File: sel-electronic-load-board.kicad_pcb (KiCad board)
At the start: 4 copper layers, 0 parts

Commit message: start laying out components : connectors and DMM bypass toggle
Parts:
- added C1: 0.1uF, Capacitor_SMD:C_1206_3216Metric_Pad1.33x1.80mm_HandSolder, F.Cu at (280.0, 70.0)
- added C2: 0.1uF, Capacitor_SMD:C_1206_3216Metric_Pad1.33x1.80mm_HandSolder, F.Cu at (266.0, 80.2)
- added C3: 0.1uF, Capacitor_SMD:C_1206_3216Metric_Pad1.33x1.80mm_HandSolder, F.Cu at (272.9, 75.5)
- added C4: 0.1uF, Capacitor_SMD:C_1206_3216Metric_Pad1.33x1.80mm_HandSolder, F.Cu at (261.9, 87.9)
- added C5: 0.1uF, Capacitor_SMD:C_1206_3216Metric_Pad1.33x1.80mm_HandSolder, F.Cu at (255.8, 87.9)
- added F1: Fuse 4A, Fuse:Fuseholder_Cylinder-5x20mm_Stelvio-Kontek_PTF78_Horizontal_Open, F.Cu at (210.8, 47.1)
- added H1: DUT+, MountingHole:MountingHole_4.3mm_M4_Pad, F.Cu at (150.0, 57.0)
- added H2: DUT-, MountingHole:MountingHole_4.3mm_M4_Pad, F.Cu at (165.0, 57.0)
- added H3: DMM+, MountingHole:MountingHole_4.3mm_M4_Pad, F.Cu at (193.0, 110.0)
- added H4: DMM-, MountingHole:MountingHole_4.3mm_M4_Pad, F.Cu at (193.0, 125.0)
- added H5: MountingHole, MountingHole:MountingHole_4.3mm_M4, F.Cu at (55.0, 55.0)
- added H6: MountingHole, MountingHole:MountingHole_4.3mm_M4, F.Cu at (195.0, 55.0)
- added H7: MountingHole, MountingHole:MountingHole_4.3mm_M4, F.Cu at (55.0, 145.0)
- added H8: MountingHole, MountingHole:MountingHole_4.3mm_M4, F.Cu at (195.0, 145.0)
- added J1: HE10 receptacle, Connector_IDC:IDC-Header_2x05_P2.54mm_Horizontal, F.Cu at (186.0, 67.0)
- added JP1: If needed by the IC, Jumper:SolderJumper-2_P1.3mm_Open_RoundedPad1.0x1.5mm, F.Cu at (227.8, 72.2)
- added Q1: N-mosfet, Package_TO_SOT_THT:TO-220-3_Vertical, F.Cu at (211.7, 84.9)
- added Q10: N-mosfet, Package_TO_SOT_THT:TO-220-3_Vertical, F.Cu at (240.4, 61.3)
- added Q11: N-mosfet, Package_TO_SOT_THT:TO-220-3_Vertical, F.Cu at (252.0, 57.5)
- added Q12: N-mosfet, Package_TO_SOT_THT:TO-220-3_Vertical, F.Cu at (234.8, 74.4)
- added Q13: N-mosfet, Package_TO_SOT_THT:TO-220-3_Vertical, F.Cu at (223.2, 84.9)
- added Q14: N-mosfet, Package_TO_SOT_THT:TO-220-3_Vertical, F.Cu at (254.6, 51.5)
- added Q15: N-mosfet, Package_TO_SOT_THT:TO-220-3_Vertical, F.Cu at (266.2, 45.5)
- added Q16: N-mosfet, Package_TO_SOT_THT:TO-220-3_Vertical, F.Cu at (266.2, 51.5)
- added Q2: N-mosfet, Package_TO_SOT_THT:TO-220-3_Vertical, F.Cu at (240.4, 55.3)
- added Q3: N-mosfet, Package_TO_SOT_THT:TO-220-3_Vertical, F.Cu at (228.9, 68.4)
- added Q4: N-mosfet, Package_TO_SOT_THT:TO-220-3_Vertical, F.Cu at (254.6, 45.5)
- added Q5: N-mosfet, Package_TO_SOT_THT:TO-220-3_Vertical, F.Cu at (228.9, 62.5)
- added Q6: N-mosfet, Package_TO_SOT_THT:TO-220-3_Vertical, F.Cu at (228.9, 56.5)
- added Q7: N-mosfet, Package_TO_SOT_THT:TO-220-3_Vertical, F.Cu at (223.2, 78.9)
- added Q8: N-mosfet, Package_TO_SOT_THT:TO-220-3_Vertical, F.Cu at (211.7, 78.9)
- added Q9: N-mosfet, Package_TO_SOT_THT:TO-220-3_Vertical, F.Cu at (240.4, 67.2)
- added RN1: 10K, Resistor_SMD:R_Array_Convex_4x0603, F.Cu at (271.1, 80.9)
- added RN2: 10K, Resistor_SMD:R_Array_Convex_4x0603, F.Cu at (245.2, 71.6)
- added RN3: 10K, Resistor_SMD:R_Array_Convex_4x0603, F.Cu at (279.1, 74.0)
- added RV1: 50K, Potentiometer_THT:Potentiometer_Bourns_3296Y_Vertical, F.Cu at (239.7, 84.7)
- added RV2: 50K, Potentiometer_THT:Potentiometer_Bourns_3296Y_Vertical, F.Cu at (282.6, 43.5)
- added RV3: 50K, Potentiometer_THT:Potentiometer_Bourns_3296Y_Vertical, F.Cu at (239.7, 78.3)
- added RV4: 50K, Potentiometer_THT:Potentiometer_Bourns_3296Y_Vertical, F.Cu at (256.9, 61.4)
- added SW1: DMM bypass, switches:toggle-switch-P4.70mm-3pins-75mils-vias, F.Cu at (193.0, 93.0)
- added U1: OpAmp, Package_SO:TSSOP-8_3x3mm_P0.65mm, F.Cu at (266.5, 76.2)
- added U2: Input stage, Package_SO:TSSOP-8_3x3mm_P0.65mm, F.Cu at (273.5, 70.7)
- added U3: Output stage, Package_SO:TSSOP-8_3x3mm_P0.65mm, F.Cu at (289.1, 44.0)
- added U4: Current sensor, Package_SO:SOIC-8_3.9x4.9mm_P1.27mm, F.Cu at (288.9, 51.2)
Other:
- board outline added: 150 x 100 mm
- board text added: "Bypass DMM"

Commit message: reorganize copper pour, traces, DMM and bypass, connector to main board
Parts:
- moved Q4 187.7 mm to (68.0, 66.0), turned to 90 degrees
- moved Q2 182.8 mm to (68.0, 116.0), turned to 90 degrees
- moved Q5 165.7 mm to (83.0, 141.0), turned to 90 degrees
- moved Q3 162.5 mm to (68.0, 91.0), turned to 90 degrees
- moved RV2 160.6 mm to (155.0, 141.0)
- moved Q9 160.4 mm to (98.0, 141.0), turned to 90 degrees
- moved Q15 159.8 mm to (113.0, 91.0), turned to 90 degrees
- moved Q11 157.6 mm to (98.0, 91.0), turned to 90 degrees
- moved Q6 157.5 mm to (83.0, 116.0), turned to 90 degrees
- moved Q14 155.6 mm to (113.0, 116.0), turned to 90 degrees
- moved Q1 154.2 mm to (68.0, 141.0), turned to 90 degrees
- moved Q16 153.8 mm to (113.0, 66.0), turned to 90 degrees
- moved Q10 152.6 mm to (98.0, 116.0), turned to 90 degrees
- moved U3 145.1 mm to (162.0, 114.0)
- moved C1 144.7 mm to (147.0, 127.0), turned to 180 degrees
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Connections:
- RN1 pad 1: Net-(RN1-Pad1) -> /SINK_CMD
- RN1 pad 5: /SINK_CMD -> Net-(RN1-Pad5)
- RN1 pad 6: Net-(RN1-Pad4) -> Net-(RN1-Pad5)
- RN2 pad 1: Net-(RN1-Pad3) -> Net-(RN1-Pad2)
- RN2 pad 8: Net-(RN1-Pad7) -> Net-(RN1-Pad5)
- RV1 pad 2: Net-(RN1-Pad1) -> Net-(RN1-Pad3)
- RV2 pad 2: Net-(RN1-Pad2) -> Net-(RN1-Pad4)
- U1 pad 1: Net-(RN1-Pad3) -> Net-(RN1-Pad2)
- U1 pad 2: Net-(RN1-Pad7) -> Net-(RN1-Pad5)
- U1 pad 6: Net-(RN1-Pad4) -> Net-(RN1-Pad7)
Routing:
- net /SINK+: track 0.00 -> 425.1 mm
- net /SINK_CMD: track 0.00 -> 284.6 mm
- net Net-(F1-Pad1): track 0.00 -> 102.7 mm
- net Net-(H4-Pad1): track 0.00 -> 78.4 mm
- net Net-(RN1-Pad4): track 0.00 -> 19.5 mm
- net Net-(RN1-Pad2): track 0.00 -> 16.5 mm
- net Net-(RN1-Pad3): track 0.00 -> 15.3 mm
- net GND: track 0.00 -> 13.7 mm, vias 0 -> 6
- net Net-(F1-Pad2): track 0.00 -> 11.4 mm
- net Net-(RN1-Pad5): track 0.00 -> 11.4 mm
- net VCC: track 0.00 -> 6.08 mm, vias 0 -> 2
- net Net-(RN1-Pad7): track 0.00 -> 5.91 mm
- net Net-(JP1-Pad2): track 0.00 -> 3.11 mm
- added copper zone on F.Cu, net /SINK+
- added copper zone on In1.Cu, net GND
- added copper zone on F.Cu, net VCC
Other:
- net class 2A: clearance 0.2 -> 0.3
- net class 3A: clearance 0.2 -> 0.4
- net class 4A: clearance 0.2 -> 0.5
- board text added: "Bias"
- board text added: "Command"
- board text added: "Gain"
- board text added: "Monitoring"
- board text added: "Offset"
- board text added: "Scale"

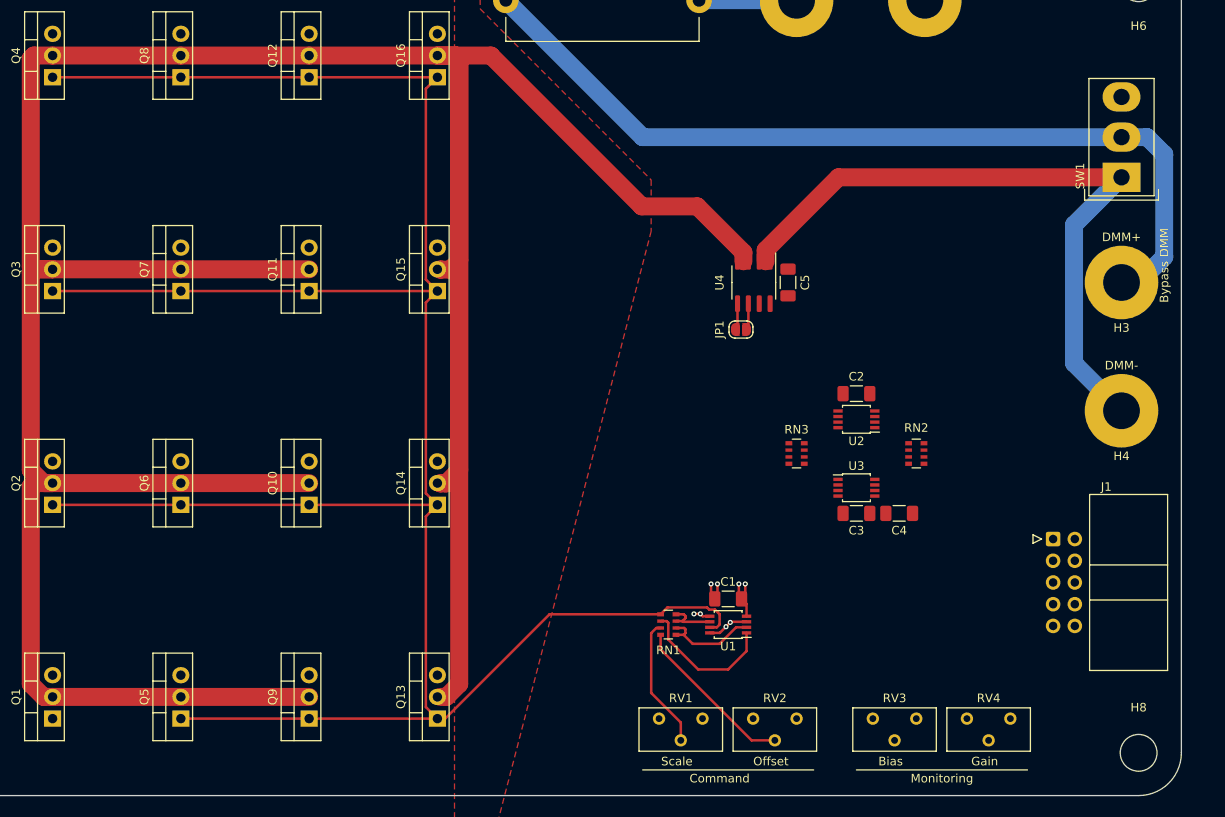
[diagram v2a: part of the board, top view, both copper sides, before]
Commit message: done tracing, optimizing the use of network resistors units
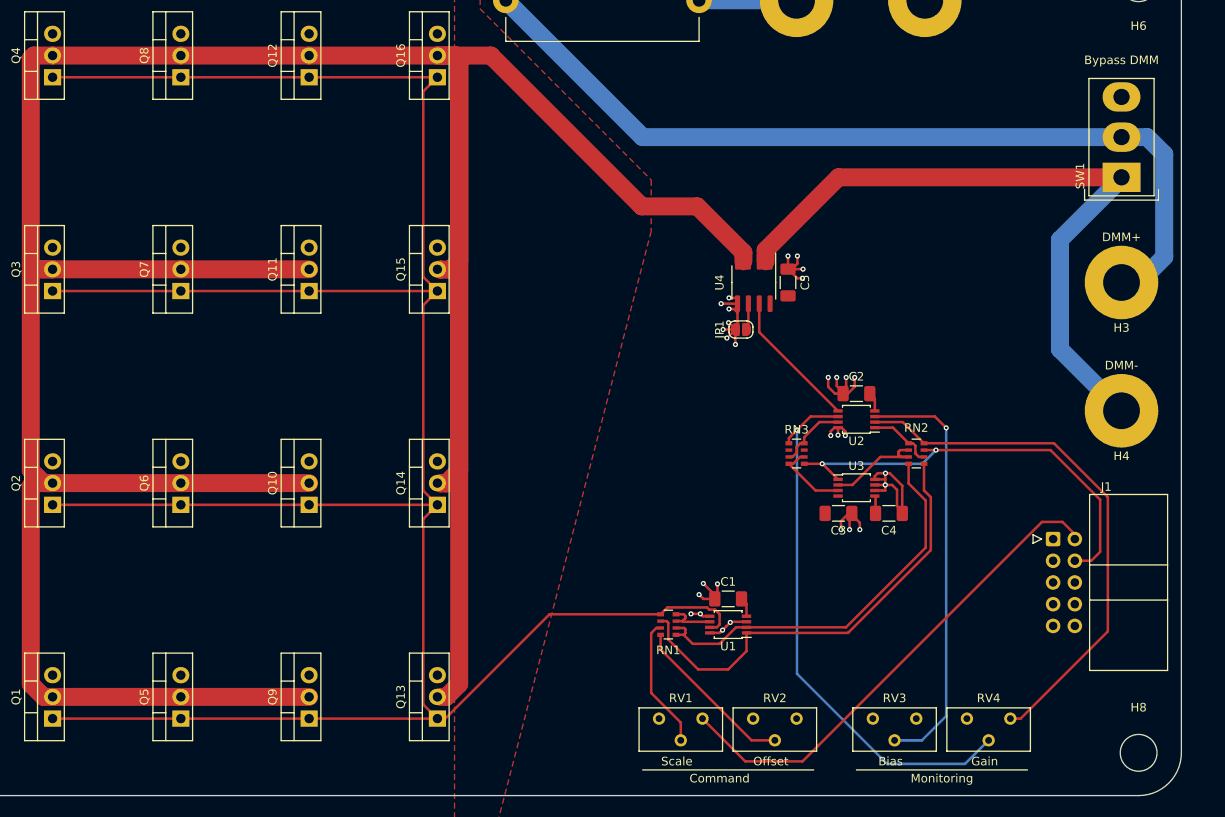
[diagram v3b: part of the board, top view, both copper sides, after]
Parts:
- moved C3 2.10 mm to (159.9, 117.0)
- moved C4 1.20 mm to (165.8, 117.0)
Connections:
- RN2 pad 4: Net-(RN2-Pad2) -> Net-(RN2-Pad4)
- RN2 pad 5: Net-(RN2-Pad5) -> Net-(RN2-Pad2)
- RN3 pad 2: Net-(RN3-Pad1) -> Net-(RN3-Pad2)
- RN3 pad 3: /UC_ADC -> Net-(RN3-Pad3)
- RN3 pad 4: (no net) -> Net-(RN3-Pad4)
- RN3 pad 5: (no net) -> /UC_ADC
- RN3 pad 6: Net-(RN3-Pad6) -> Net-(RN3-Pad4)
- RN3 pad 7: Net-(RN3-Pad6) -> Net-(RN3-Pad7)
- RN3 pad 8: Net-(RN3-Pad8) -> Net-(RN3-Pad3)
- RV4 pad 1: Net-(RN2-Pad5) -> Net-(RN2-Pad4)
- RV4 pad 2: Net-(RN3-Pad8) -> Net-(RN3-Pad1)
- U2 pad 2: Net-(RN2-Pad5) -> Net-(RN2-Pad4)
- U2 pad 6: Net-(RN3-Pad8) -> Net-(RN3-Pad1)
- U2 pad 7: Net-(RN3-Pad1) -> Net-(RN3-Pad3)
- U3 pad 3: Net-(RN3-Pad6) -> Net-(RN3-Pad4)
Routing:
- net Net-(RN3-Pad1): track 0.00 -> 63.8 mm, vias 0 -> 1
- net Net-(RN2-Pad4): track 0.00 -> 62.2 mm
- net GND: track 13.7 -> 73.7 mm, vias 6 -> 30
- net /UC_DAC: track 0.00 -> 58.4 mm
- net /UC_ADC: track 0.00 -> 51.2 mm, vias 0 -> 2
- net Net-(RV3-Pad2): track 0.00 -> 49.8 mm, vias 0 -> 1
- net Net-(RN1-Pad2): track 16.5 -> 52.5 mm
- net Net-(RN1-Pad5): track 11.4 -> 46.8 mm
- net /V_SENSE: track 0.00 -> 16.4 mm
- net /SINK_CMD: track 284.6 -> 300.3 mm
- net Net-(RN2-Pad6): track 0.00 -> 12.5 mm
- net Net-(RN3-Pad4): track 0.00 -> 9.18 mm
- net Net-(RN3-Pad3): track 0.00 -> 8.23 mm
- net Net-(RN2-Pad2): track 0.00 -> 7.70 mm
- net Net-(C4-Pad1): track 0.00 -> 2.06 mm
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
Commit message: prepare first release
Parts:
- added G***: LOGO, cliparts:logo--cc--zero, F.Cu at (125.0, 100.0)
- added G***: LOGO, cliparts:logo--cc--cc, F.Cu at (120.0, 100.0)
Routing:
- net VCC: vias 0 -> 3
- net GND: vias 30 -> 33
- added copper zone on B.Cu, net /SINK+
- added copper zone on In2.Cu, net GND
- added copper zone on B.Cu, net VCC
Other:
- board text added: "WITHOUT ANY WARRANTY OF ANY KIND, INCLUDING, BUT NOT LIMITED TO, THE IMPLIED WARRANTIES OF SAFETY, MERCHANTABILITY AND FITNESS FOR A PARTICULAR PURPOSE."
- board text added: "https://github.com/sporniket/sel-electronic-load-board v0.0.1"

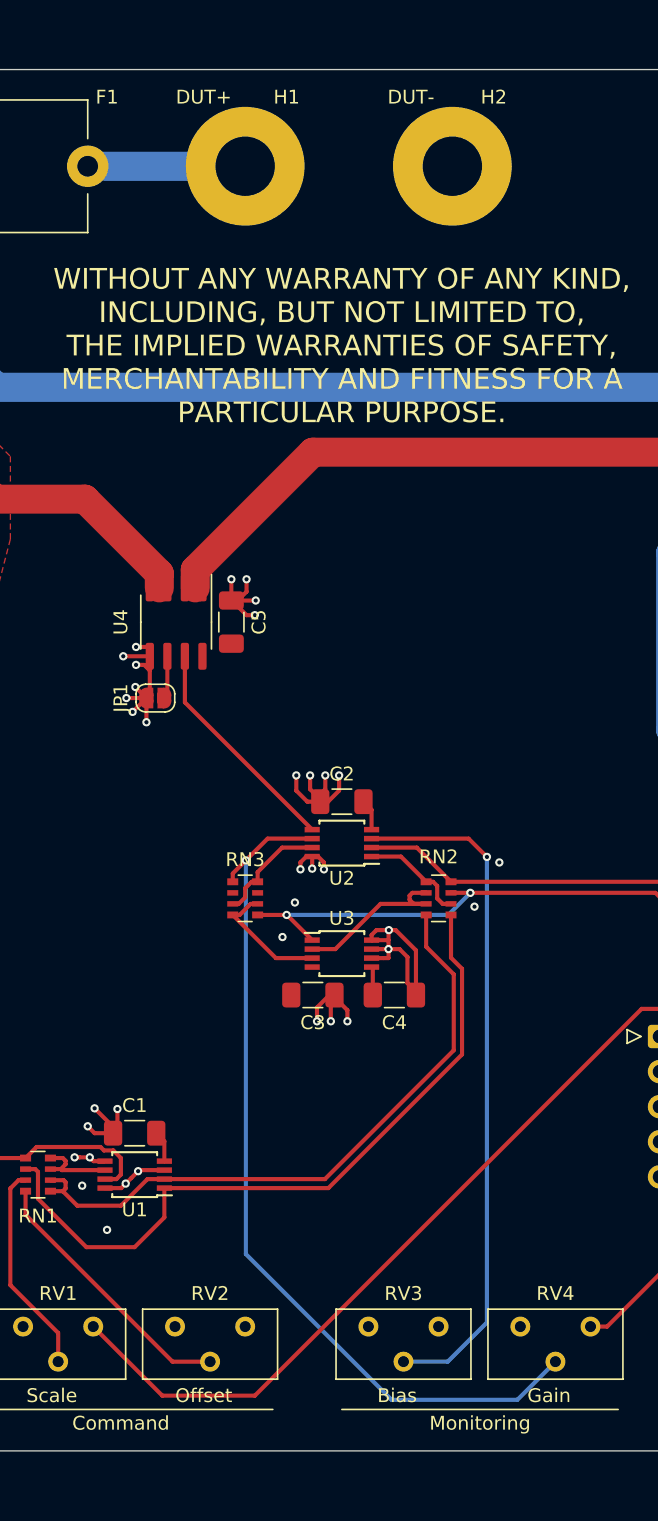
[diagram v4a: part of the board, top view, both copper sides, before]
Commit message: adjust labels on silkscreen
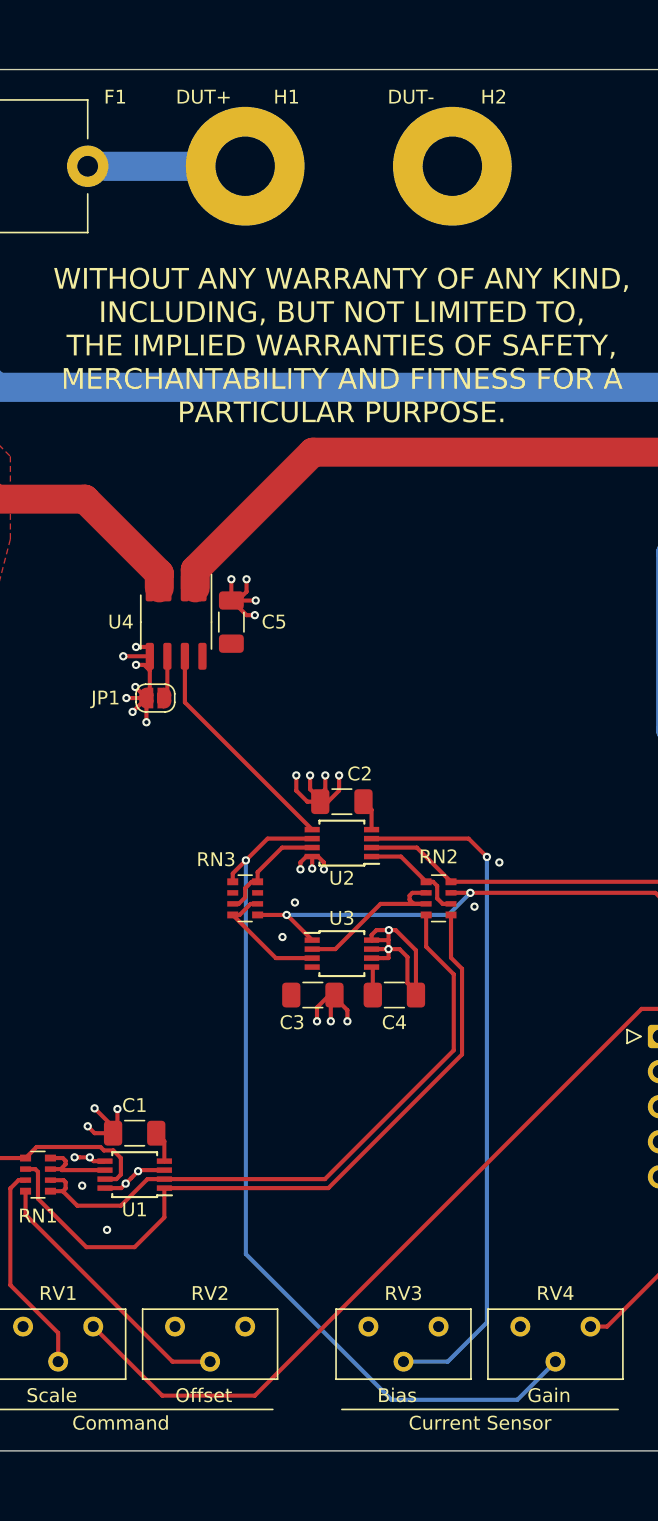
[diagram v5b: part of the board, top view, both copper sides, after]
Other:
- board text added: "Current Sensor"
- board text removed: "Monitoring"
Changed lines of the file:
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@@
     (tags "SOIC SO")
     (attr smd)
-    (fp_text reference U4 (at 0 4 90) (layer F.SilkS)
+    (fp_text reference U4 (at 0 4 180) (layer F.SilkS)
       (effects (font (size 1 1) (thickness 0.15)))
     )
@@
     (tags "resistor array")
     (attr smd)
-    (fp_text reference RN3 (at 0 -2.8) (layer F.SilkS)
+    (fp_text reference RN3 (at -2.1 -2.8) (layer F.SilkS)
       (effects (font (size 1 1) (thickness 0.15)))
     )
@@
     (tags "solder jumper open")
     (attr virtual)
-    (fp_text reference JP1 (at -2.5 0 270) (layer F.SilkS)
+    (fp_text reference JP1 (at -3.6 0) (layer F.SilkS)
       (effects (font (size 1 1) (thickness 0.15)))
     )
@@
     (descr https://www.tme.eu/en/Document/3b48dbe2b9714a62652c97b08fcd464b/PTF78.pdf)
     (tags "Fuseholder horizontal open 5x20 Stelvio-Kontek PTF/78")
-    (fp_text reference F1 (at 24 -5) (layer F.SilkS)
+    (fp_text reference F1 (at 24.6 -5) (layer F.SilkS)
       (effects (font (size 1 1) (thickness 0.15)))
     )
@@
     (tags "capacitor handsolder")
     (attr smd)
-    (fp_text reference C5 (at 0 2 90) (layer F.SilkS)
+    (fp_text reference C5 (at 0 3.1 180) (layer F.SilkS)
       (effects (font (size 1 1) (thickness 0.15)))
     )
@@
     (tags "capacitor handsolder")
     (attr smd)
-    (fp_text reference C3 (at 0 2) (layer F.SilkS)
+    (fp_text reference C3 (at -1.5 2) (layer F.SilkS)
       (effects (font (size 1 1) (thickness 0.15)))
     )
@@
     (tags "capacitor handsolder")
     (attr smd)
-    (fp_text reference C2 (at 0 2) (layer F.SilkS)
+    (fp_text reference C2 (at -1.3 2) (layer F.SilkS)
       (effects (font (size 1 1) (thickness 0.15)))
     )
@@
     (effects (font (size 1 1) (thickness 0.15)))
   )
-  (gr_text Monitoring (at 172 148) (layer F.SilkS)
+  (gr_text "Current Sensor" (at 172 148) (layer F.SilkS)
     (effects (font (size 1 1) (thickness 0.15)))
   )
